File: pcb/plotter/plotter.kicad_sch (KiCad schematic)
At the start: 42 parts, among them J1 SH 1106 Display, J10 Limit switches, J11 GRBL switches???, J2 SWD, J3 Console, J4 Micro_SD_Card_Det, J5 USB_B_Micro, J7 Servo, SW1 Rotary_Encoder_Switch, U1 STM32F405RGTx, U4 MIC5504-3.3YM5

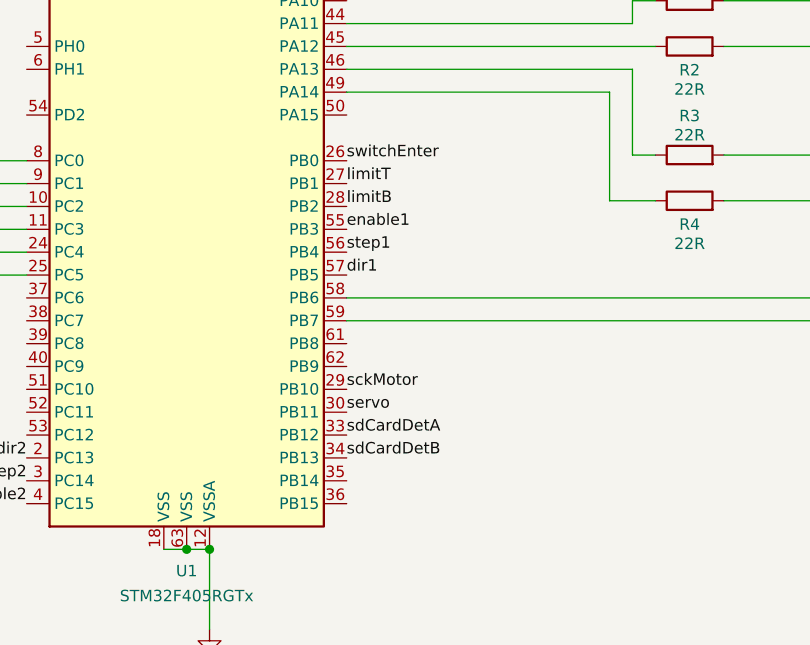
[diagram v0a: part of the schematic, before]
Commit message: Moving to STM32F405 and the final pinout (as on the PCB in the future).
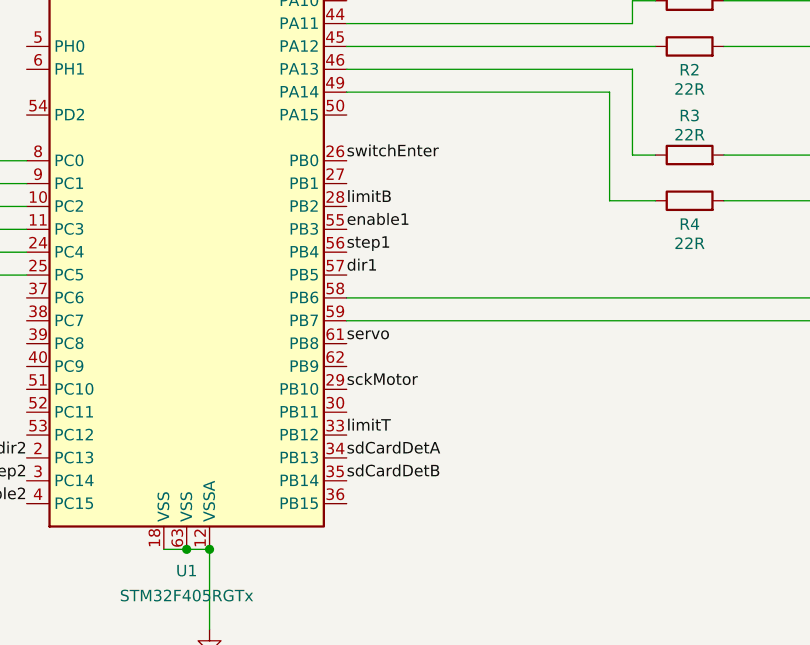
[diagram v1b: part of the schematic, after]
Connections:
- net limitT: now also U1.33 (PB12); no longer U1.27 (PB1)
- net sdCardDetA: now also U1.34 (PB13); no longer U1.33 (PB12)
- net sdCardDetB: now also U1.35 (PB14); no longer U1.34 (PB13)
- net servo: now also U1.61 (PB8); no longer U1.30 (PB11)
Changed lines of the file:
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@@
-    (effects (font (size 1.27 1.27)) (justify left bottom))
-  )
-  (label "limitT" (at 174.625 104.14 0)
     (effects (font (size 1.27 1.27)) (justify left bottom))
   )
@@
     (effects (font (size 1.27 1.27)) (justify left bottom))
   )
+  (label "servo" (at 174.625 121.92 0)
+    (effects (font (size 1.27 1.27)) (justify left bottom))
+  )
   (label "sckMotor" (at 174.625 127 0)
     (effects (font (size 1.27 1.27)) (justify left bottom))
   )
-  (label "servo" (at 174.625 129.54 0)
+  (label "limitT" (at 174.625 132.08 0)
     (effects (font (size 1.27 1.27)) (justify left bottom))
   )
-  (label "sdCardDetA" (at 174.625 132.08 0)
+  (label "sdCardDetA" (at 174.625 134.62 0)
     (effects (font (size 1.27 1.27)) (justify left bottom))
   )
-  (label "sdCardDetB" (at 174.625 134.62 0)
+  (label "sdCardDetB" (at 174.625 137.16 0)
     (effects (font (size 1.27 1.27)) (justify left bottom))
   )
@@
   (symbol (lib_id "power:VDD") (at 222.25 38.735 90) (unit 1)
     (in_bom yes) (on_board yes) (fields_autoplaced)
-    (property "Reference" "#PWR?" (id 0) (at 226.06 38.735 0)
+    (property "Reference" "#PWR0121" (id 0) (at 226.06 38.735 0)
       (effects (font (size 1.27 1.27)) hide)
     )
@@
   (symbol (lib_id "power:GND") (at 222.25 43.815 270) (mirror x) (unit 1)
     (in_bom yes) (on_board yes) (fields_autoplaced)
-    (property "Reference" "#PWR?" (id 0) (at 215.9 43.815 0)
+    (property "Reference" "#PWR0122" (id 0) (at 215.9 43.815 0)
       (effects (font (size 1.27 1.27)) hide)
     )
@@
   (symbol (lib_id "power:GND") (at 268.605 53.975 0) (mirror y) (unit 1)
     (in_bom yes) (on_board yes) (fields_autoplaced)
-    (property "Reference" "#PWR?" (id 0) (at 268.605 60.325 0)
+    (property "Reference" "#PWR0123" (id 0) (at 268.605 60.325 0)
       (effects (font (size 1.27 1.27)) hide)
     )
@@
       (reference "#PWR0120") (unit 1) (value "+5V") (footprint "")
     )
+    (path "/21a3c08e-04d8-4de5-b61f-086267da260c"
+      (reference "#PWR0121") (unit 1) (value "VDD") (footprint "")
+    )
+    (path "/d51d9554-3c94-4581-aff4-1c8667ec8b63"
+      (reference "#PWR0122") (unit 1) (value "GND") (footprint "")
+    )
     (path "/11260e23-ae37-4e36-962e-fd2aad3489c3"
-      (reference "#PWR?") (unit 1) (value "GND") (footprint "")
-    )
-    (path "/21a3c08e-04d8-4de5-b61f-086267da260c"
-      (reference "#PWR?") (unit 1) (value "VDD") (footprint "")
-    )
-    (path "/d51d9554-3c94-4581-aff4-1c8667ec8b63"
-      (reference "#PWR?") (unit 1) (value "GND") (footprint "")
+      (reference "#PWR0123") (unit 1) (value "GND") (footprint "")
     )
     (path "/c73a8afd-1bb2-4582-b865-0602b4353a4c"

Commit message: PCB and 3d model. Still work in progress.
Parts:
- removed D1, D2, D3: D_TVS, symbol Device:D_TVS
- removed J11: GRBL switches???, Connector_PinHeader_2.54mm:PinHeader_1x04_P2.54mm_Vertical, symbol Connector:Conn_01x04_Male
- removed J7: Servo, Connector_PinHeader_2.54mm:PinHeader_1x03_P2.54mm_Vertical, symbol Connector:Conn_01x03_Male
- removed U4: MIC5504-3.3YM5, Package_TO_SOT_SMD:SOT-23-5, symbol Regulator_Linear:MIC5504-3.3YM5
- added C38, C39, C40, C41, C42, C43, C44, C45: 100nF, Capacitor_SMD:C_0603_1608Metric, symbol Device:C
- added R10, R11, R5, R6, R7, R8, R9: 1k, Resistor_SMD:R_0603_1608Metric, symbol Device:R
- added U4, U7, U8: PUSB3F96, Package_DFN_QFN:Diodes_UDFN-10_1.0x2.5mm_P0.5mm, symbol iwasz:PUSB3F96
- added U6: AP1117-33, Package_TO_SOT_SMD:SOT-223-3_TabPin2, symbol Regulator_Linear:AP1117-33
- C1: footprint Capacitor_THT:CP_Radial_D13.0mm_P5.00mm -> Capacitor_SMD:CP_Elec_8x10
- J1: footprint Connector_PinHeader_2.54mm:PinHeader_1x04_P2.54mm_Vertical -> iwasz:SH1106
- J10: footprint Connector_PinHeader_2.54mm:PinHeader_1x05_P2.54mm_Vertical -> Connector_JST:JST_PH_B8B-PH-K_1x08_P2.00mm_Vertical; symbol Connector:Conn_01x05_Male -> Connector:Conn_01x08_Male
- J4: footprint Connector_Card:microSD_HC_Hirose_DM3AT-SF-PEJM5 -> iwasz:microSD_HC_Hirose_DM3AT-SF-PEJM5
- J5: footprint Connector_USB:USB_Micro-B_Amphenol_10104110_Horizontal -> iwasz:USB_Micro-B_Amphenol_10104110_Horizontal
- SW1: footprint Rotary_Encoder:RotaryEncoder_Alps_EC11E-Switch_Vertical_H20mm -> iwasz:RotaryEncoder_Alps_EC11E_Vertical_H20mm
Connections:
- net +5V: now also J10.7 (Pin_7), U6.3 (VI)
- net GND: now also C36.1, J10.8 (Pin_8), J5.6 (Shield), SW1.C, C38.1, C39.2, C40.2, C41.2, C42.1, C43.1, C44.1, C45.1, U4.3 (GND), U4.8 (GND), U6.1 (GND), U7.3 (GND), U7.8 (GND), U8.3 (GND), U8.8 (GND)
- net VDD: now also C36.2, C38.2, U6.2 (VO)
- net limitB: now also C45.2, R11.2; no longer J10.4 (Pin_4)
- net limitL: now also C42.2, R8.2; no longer J10.1 (Pin_1)
- net limitR: now also C43.2, R9.2; no longer J10.2 (Pin_2)
- net limitT: now also C44.2, R10.2; no longer J10.3 (Pin_3)
- net servo: now also J10.6 (Pin_6)
- net switchEnter: now also C39.1, R5.1, U4.1; no longer SW1.S1
- net at J4.2 (DAT3/CD), U1.20 (PA4): now also U7.5
- net at J4.3 (CMD): now also U1.23 (PA7), U7.4
- net at J4.5 (CLK), U1.21 (PA5): now also U7.2
- net at J4.7 (DAT0), U1.22 (PA6): now also U7.1
- net at J4.8 (DAT1): no longer U1.23 (PA7)
- net at J5.2 (D-), R1.2: now also U8.2
- net at J5.3 (D+), R2.2: now also U8.1
- net at U1.24 (PC4): now also C40.1, R6.1; no longer SW1.A
- net at U1.25 (PC5): now also C41.1, R7.1; no longer SW1.B
- net sdCardDetA renamed esd1
- net esd1: now also U8.5
- net sdCardDetB renamed esd2
- net esd2: now also U8.4
- new net: R5.2, SW1.S1
- new net: J10.4 (Pin_4), R11.1
- new net: J10.1 (Pin_1), R8.1
- new net: J10.2 (Pin_2), R9.1
- new net: J10.3 (Pin_3), R10.1
- new net esd3: R6.2, SW1.A, U4.2
- new net esd4: R7.2, SW1.B, U4.4
- no-connect marks 2 -> 4
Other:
- note removed: "May be to small for µC, OLED & SD."
- note removed: "TODO"
- moved on the sheet: C1, C36, J3

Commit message: Thread priorites.
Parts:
- added R12: 22R, Resistor_SMD:R_0603_1608Metric, symbol Device:R
- added TP1: Reset, TestPoint:TestPoint_Pad_1.5x1.5mm, symbol Connector:TestPoint
- U4, U7, U8: footprint Package_DFN_QFN:Diodes_UDFN-10_1.0x2.5mm_P0.5mm -> iwasz:Diodes_UDFN-10_1.0x2.5mm_P0.5mm
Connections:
- net GND: now also R12.1
- net at U1.60 (BOOT0): now also R12.2
- net at U1.7 (NRST): now also TP1.1
- no-connect marks 4 -> 23
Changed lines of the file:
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@@
   (junction (at 225.425 88.9) (diameter 1.016) (color 0 0 0 0))
   (junction (at 227.965 83.82) (diameter 1.016) (color 0 0 0 0))
-  (junction (at 251.46 77.47) (diameter 1.016) (color 0 0 0 0))
+  (no_connect (at 97.79 146.05))
+  (no_connect (at 139.065 88.9))
+  (no_connect (at 139.065 91.44))
+  (no_connect (at 139.065 96.52))
+  (no_connect (at 139.065 116.84))
+  (no_connect (at 139.065 119.38))
+  (no_connect (at 139.065 121.92))
+  (no_connect (at 139.065 124.46))
+  (no_connect (at 139.065 127))
+  (no_connect (at 139.065 129.54))
+  (no_connect (at 139.065 132.08))
+  (no_connect (at 174.625 78.74))
+  (no_connect (at 174.625 81.28))
+  (no_connect (at 174.625 83.82))
+  (no_connect (at 174.625 96.52))
+  (no_connect (at 174.625 104.14))
+  (no_connect (at 174.625 124.46))
+  (no_connect (at 174.625 129.54))
+  (no_connect (at 174.625 139.7))
   (no_connect (at 225.425 31.115))
   (no_connect (at 225.425 48.895))
@@
     (stroke (width 0) (type solid) (color 0 0 0 0))
   )
+  (wire (pts (xy 127 63.5) (xy 128.27 63.5))
+    (stroke (width 0) (type solid) (color 0 0 0 0))
+  )
   (wire (pts (xy 132.08 71.12) (xy 132.08 72.39))
     (stroke (width 0) (type solid) (color 0 0 0 0))
@@
     (stroke (width 0) (type solid) (color 0 0 0 0))
   )
+  (wire (pts (xy 135.89 63.5) (xy 139.065 63.5))
+    (stroke (width 0) (type solid) (color 0 0 0 0))
+  )
   (wire (pts (xy 139.065 68.58) (xy 121.92 68.58))
     (stroke (width 0) (type solid) (color 0 0 0 0))
@@
     (stroke (width 0) (type solid) (color 0 0 0 0))
   )
-  (wire (pts (xy 254 77.47) (xy 251.46 77.47))
+  (wire (pts (xy 254 76.2) (xy 254 77.47))
     (stroke (width 0) (type solid) (color 0 0 0 0))
   )
@@
     )
     (property "Datasheet" "" (id 3) (at 247.65 108.585 0)
+      (effects (font (size 1.27 1.27)) hide)
+    )
+    (pin "1")
+  )
+  (symbol (lib_id "Connector:TestPoint") (at 139.065 58.42 0) (unit 1)
+    (in_bom yes) (on_board yes) (fields_autoplaced)
+    (property "Reference" "TP1" (id 0) (at 140.4621 55.67 0)
+      (effects (font (size 1.27 1.27)) (justify left))
+    )
+    (property "Value" "Reset" (id 1) (at 140.4621 58.4451 0)
+      (effects (font (size 1.27 1.27)) (justify left))
+    )
+    (property "Footprint" "TestPoint:TestPoint_Pad_1.5x1.5mm" (id 2) (at 144.145 58.42 0)
+      (effects (font (size 1.27 1.27)) hide)
+    )
+    (property "Datasheet" "~" (id 3) (at 144.145 58.42 0)
       (effects (font (size 1.27 1.27)) hide)
     )
@@
     (pin "1")
   )
+  (symbol (lib_id "power:GND") (at 127 63.5 270) (unit 1)
+    (in_bom yes) (on_board yes) (fields_autoplaced)
+    (property "Reference" "#PWR0128" (id 0) (at 120.65 63.5 0)
+      (effects (font (size 1.27 1.27)) hide)
+    )
+    (property "Value" "GND" (id 1) (at 128.0161 63.979 90)
+      (effects (font (size 1.27 1.27)) (justify left))
+    )
+    (property "Footprint" "" (id 2) (at 127 63.5 0)
+      (effects (font (size 1.27 1.27)) hide)
+    )
+    (property "Datasheet" "" (id 3) (at 127 63.5 0)
+      (effects (font (size 1.27 1.27)) hide)
+    )
+    (pin "1")
+  )
   (symbol (lib_id "power:GND") (at 159.385 153.67 0) (unit 1)
     (in_bom yes) (on_board yes) (fields_autoplaced)
@@
     )
     (property "Datasheet" "" (id 3) (at 251.46 76.2 0)
+      (effects (font (size 1.27 1.27)) hide)
+    )
+    (pin "1")
+  )
+  (symbol (lib_id "power:GND") (at 254 76.2 0) (mirror x) (unit 1)
+    (in_bom yes) (on_board yes) (fields_autoplaced)
+    (property "Reference" "#PWR026" (id 0) (at 254 69.85 0)
+      (effects (font (size 1.27 1.27)) hide)
+    )
+    (property "Value" "GND" (id 1) (at 252.095 75.5995 0)
+      (effects (font (size 1.27 1.27)) (justify right))
+    )
+    (property "Footprint" "" (id 2) (at 254 76.2 0)
+      (effects (font (size 1.27 1.27)) hide)
+    )
+    (property "Datasheet" "" (id 3) (at 254 76.2 0)
       (effects (font (size 1.27 1.27)) hide)
     )
@@
     )
     (property "Datasheet" "~" (id 3) (at 107.95 129.54 0)
+      (effects (font (size 1.27 1.27)) hide)
+    )
+    (pin "1")
+    (pin "2")
+  )
+  (symbol (lib_id "Device:R") (at 132.08 63.5 90) (unit 1)
+    (in_bom yes) (on_board yes) (fields_autoplaced)
+    (property "Reference" "R12" (id 0) (at 132.08 58.5174 90))
+    (property "Value" "22R" (id 1) (at 132.08 61.2925 90))
+    (property "Footprint" "Resistor_SMD:R_0603_1608Metric" (id 2) (at 132.08 65.278 90)
+      (effects (font (size 1.27 1.27)) hide)
+    )
+    (property "Datasheet" "~" (id 3) (at 132.08 63.5 0)
       (effects (font (size 1.27 1.27)) hide)
     )
@@
       (effects (font (size 1.27 1.27)) (justify left))
     )
-    (property "Footprint" "Package_DFN_QFN:Diodes_UDFN-10_1.0x2.5mm_P0.5mm" (id 2) (at 89.535 151.13 0)
+    (property "Footprint" "iwasz:Diodes_UDFN-10_1.0x2.5mm_P0.5mm" (id 2) (at 89.535 151.13 0)
       (effects (font (size 1.27 1.27)) hide)
     )
@@
     (property "Reference" "U7" (id 0) (at 195.58 41.8042 0))
     (property "Value" "PUSB3F96" (id 1) (at 195.58 44.5793 0))
-    (property "Footprint" "Package_DFN_QFN:Diodes_UDFN-10_1.0x2.5mm_P0.5mm" (id 2) (at 195.58 52.07 0)
+    (property "Footprint" "iwasz:Diodes_UDFN-10_1.0x2.5mm_P0.5mm" (id 2) (at 195.58 52.07 0)
       (effects (font (size 1.27 1.27)) hide)
     )
@@
       (effects (font (size 1.27 1.27)) (justify left))
     )
-    (property "Footprint" "Package_DFN_QFN:Diodes_UDFN-10_1.0x2.5mm_P0.5mm" (id 2) (at 230.505 70.485 0)
+    (property "Footprint" "iwasz:Diodes_UDFN-10_1.0x2.5mm_P0.5mm" (id 2) (at 230.505 70.485 0)
       (effects (font (size 1.27 1.27)) hide)
     )
@@
       (reference "#PWR021") (unit 1) (value "GND") (footprint "")
     )
+    (path "/930b2f78-333c-4610-89f3-9407fdd532f3/a4d2715b-49f7-4e09-ada6-46c348494811"
+      (reference "#PWR022") (unit 1) (value "GND") (footprint "")
+    )
+    (path "/930b2f78-333c-4610-89f3-9407fdd532f3/19645a58-08df-44dc-ab86-f7f31a24b387"
+      (reference "#PWR023") (unit 1) (value "GND") (footprint "")
+    )
+    (path "/930b2f78-333c-4610-89f3-9407fdd532f3/a591e740-17c3-473d-a595-acd8ce4a02be"
+      (reference "#PWR024") (unit 1) (value "GND") (footprint "")
+    )
+    (path "/930b2f78-333c-4610-89f3-9407fdd532f3/90d9b658-fc5f-48df-b4fd-a0a042ffac1c"
+      (reference "#PWR025") (unit 1) (value "GND") (footprint "")
+    )
+    (path "/aa842cbf-036f-4f78-bf1e-99757779f173"
+      (reference "#PWR026") (unit 1) (value "GND") (footprint "")
+    )
     (path "/34919b94-3e82-4565-9cd3-ea2a1078c1b9"
       (reference "#PWR0101") (unit 1) (value "GND") (footprint "")
@@
       (reference "#PWR0103") (unit 1) (value "VDD") (footprint "")
     )
+    (path "/930b2f78-333c-4610-89f3-9407fdd532f3/d85fc035-0342-43b7-8cbb-4a176cb989ce"
+      (reference "#PWR0104") (unit 1) (value "+5V") (footprint "")
+    )
     (path "/930b2f78-333c-4610-89f3-9407fdd532f3/8c830d4a-0bae-4d2d-9fc6-234cbc322a45"
       (reference "#PWR0105") (unit 1) (value "+24V") (footprint "")
@@
       (reference "#PWR0106") (unit 1) (value "+24V") (footprint "")
     )
+    (path "/930b2f78-333c-4610-89f3-9407fdd532f3/3ef9afe7-2f08-451e-b959-099b3c9b949b"
+      (reference "#PWR0107") (unit 1) (value "+5V") (footprint "")
+    )
     (path "/930b2f78-333c-4610-89f3-9407fdd532f3/ff3766ff-40b1-4c32-bb2e-f6c7ba4ab4a2"
       (reference "#PWR0108") (unit 1) (value "GND") (footprint "")
@@
       (reference "#PWR0127") (unit 1) (value "GND") (footprint "")
     )
-    (path "/930b2f78-333c-4610-89f3-9407fdd532f3/3ef9afe7-2f08-451e-b959-099b3c9b949b"
-      (reference "#PWR?") (unit 1) (value "+5V") (footprint "")
-    )
-    (path "/930b2f78-333c-4610-89f3-9407fdd532f3/d85fc035-0342-43b7-8cbb-4a176cb989ce"
-      (reference "#PWR?") (unit 1) (value "+5V") (footprint "")
+    (path "/ed831ba4-9978-4ec3-9d75-2e40f038e16e"
+      (reference "#PWR0128") (unit 1) (value "GND") (footprint "")
     )
     (path "/c73a8afd-1bb2-4582-b865-0602b4353a4c"
@@
       (reference "R11") (unit 1) (value "1k") (footprint "Resistor_SMD:R_0603_1608Metric")
     )
+    (path "/9516bb37-bce1-45ba-96f6-12e1cc5efa7b"
+      (reference "R12") (unit 1) (value "22R") (footprint "Resistor_SMD:R_0603_1608Metric")
+    )
     (path "/aad9a816-7f7b-42ba-adfd-b21451a17f15"
       (reference "SW1") (unit 1) (value "Rotary_Encoder_Switch") (footprint "iwasz:RotaryEncoder_Alps_EC11E_Vertical_H20mm")
@@
       (reference "SW2") (unit 1) (value "SW_SPDT") (footprint "iwasz:MFP 201 NR_copy")
     )
+    (path "/fc11cf88-52e2-47ac-ac30-979dddf4fd5f"
+      (reference "TP1") (unit 1) (value "Reset") (footprint "TestPoint:TestPoint_Pad_1.5x1.5mm")
+    )
     (path "/b935b4c4-83fc-43de-9503-3af7021f8333"
       (reference "U1") (unit 1) (value "STM32F405RGTx") (footprint "Package_QFP:LQFP-64_10x10mm_P0.5mm")
@@
     )
     (path "/d0c210e7-b945-449f-a69a-33e60fce21d9"
-      (reference "U4") (unit 1) (value "PUSB3F96") (footprint "Package_DFN_QFN:Diodes_UDFN-10_1.0x2.5mm_P0.5mm")
+      (reference "U4") (unit 1) (value "PUSB3F96") (footprint "iwasz:Diodes_UDFN-10_1.0x2.5mm_P0.5mm")
     )
     (path "/930b2f78-333c-4610-89f3-9407fdd532f3/cb09f838-5537-4040-af14-fc9d114895c9"
@@
     )
     (path "/7eafb0a6-1343-4dc2-9c29-70ea4ba9f01e"
-      (reference "U7") (unit 1) (value "PUSB3F96") (footprint "Package_DFN_QFN:Diodes_UDFN-10_1.0x2.5mm_P0.5mm")
+      (reference "U7") (unit 1) (value "PUSB3F96") (footprint "iwasz:Diodes_UDFN-10_1.0x2.5mm_P0.5mm")
     )
     (path "/3c2feef1-2ca6-419a-9b61-04a57cdfde85"
-      (reference "U8") (unit 1) (value "PUSB3F96") (footprint "Package_DFN_QFN:Diodes_UDFN-10_1.0x2.5mm_P0.5mm")
-    )
-  )
+      (reference "U8") (unit 1) (value "PUSB3F96") (footprint "iwasz:Diodes_UDFN-10_1.0x2.5mm_P0.5mm")
+    )
+  )

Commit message: Communication with the GRBL for SD card impl.
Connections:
- net switchEnter: now also U1.37 (PC6); no longer U1.26 (PB0)
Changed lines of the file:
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@@
   (no_connect (at 139.065 91.44))
   (no_connect (at 139.065 96.52))
-  (no_connect (at 139.065 116.84))
   (no_connect (at 139.065 119.38))
   (no_connect (at 139.065 121.92))
@@
   (no_connect (at 174.625 83.82))
   (no_connect (at 174.625 96.52))
+  (no_connect (at 174.625 101.6))
   (no_connect (at 174.625 104.14))
   (no_connect (at 174.625 124.46))
@@
     (effects (font (size 1.27 1.27)) (justify left bottom))
   )
+  (label "switchEnter" (at 139.065 116.84 180)
+    (effects (font (size 1.27 1.27)) (justify right bottom))
+  )
   (label "dir2" (at 139.065 134.62 180)
     (effects (font (size 1.27 1.27)) (justify right bottom))
@@
     (effects (font (size 1.27 1.27)) (justify left bottom))
   )
-  (label "switchEnter" (at 174.625 101.6 0)
-    (effects (font (size 1.27 1.27)) (justify left bottom))
-  )
